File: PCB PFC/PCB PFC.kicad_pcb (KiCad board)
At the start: 2 copper layers, 44 parts, among them J1 INA_1, J2 INA_2, J4 External_Power, J5 BAT54S_1, J6 BAT54S_2, SW2 SW_Push, U2 L7805, U3 TL082, U4 TL084, U5 TL082, U8 ESP32-C3_SUPERMINI_TH

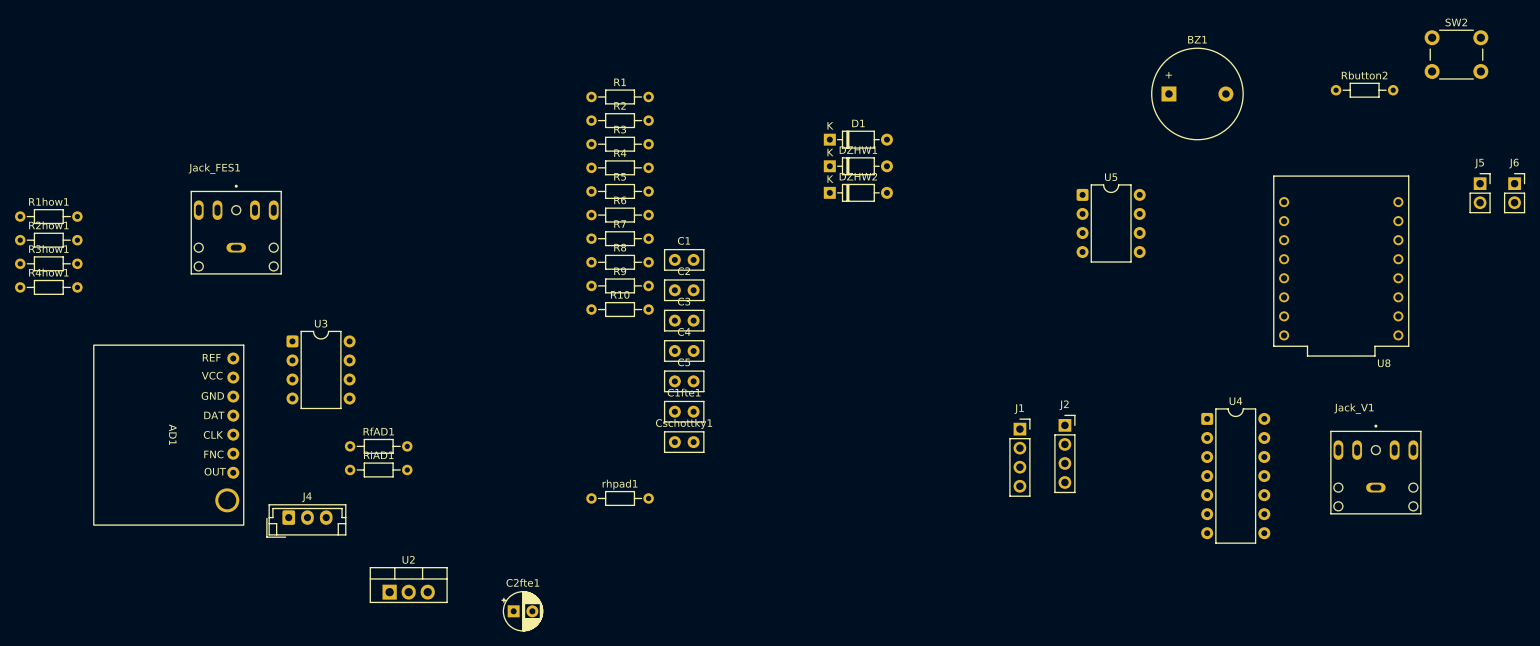
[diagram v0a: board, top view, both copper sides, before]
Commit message: Cambio valores a comerciales y agrego OpAmps SMD
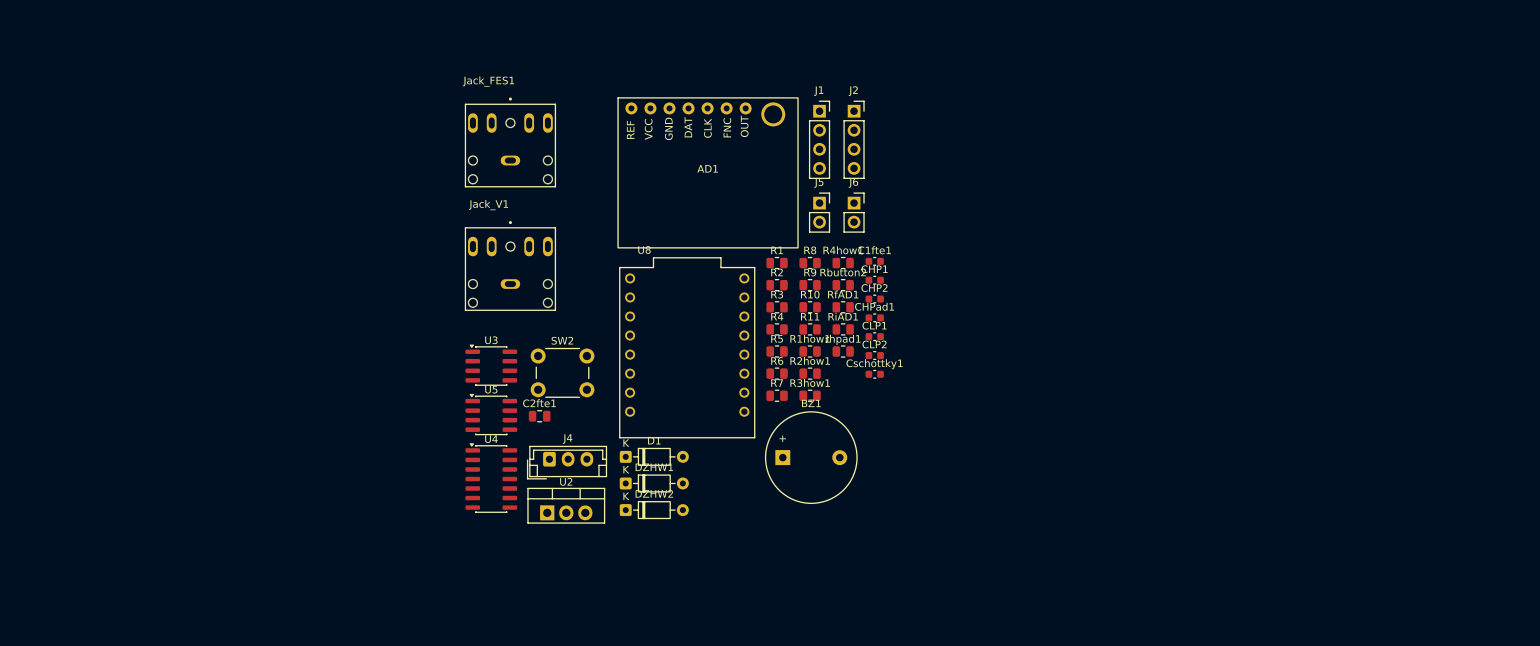
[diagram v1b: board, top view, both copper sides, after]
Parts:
- removed C1: C, Capacitor_THT:C_Disc_D5.0mm_W2.5mm_P2.50mm
- removed C2: 100n, Capacitor_THT:C_Disc_D5.0mm_W2.5mm_P2.50mm
- removed C3: 100p, Capacitor_THT:C_Disc_D5.0mm_W2.5mm_P2.50mm
- removed C4: 1.8n, Capacitor_THT:C_Disc_D5.0mm_W2.5mm_P2.50mm
- removed C5: 220p, Capacitor_THT:C_Disc_D5.0mm_W2.5mm_P2.50mm
- added CHP1: 4.7n, Capacitor_SMD:C_0603_1608Metric, F.Cu at (158.2, 85.3)
- added CHP2: 1.5n, Capacitor_SMD:C_0603_1608Metric, F.Cu at (158.2, 87.8)
- added CHPad1: 10uF, Capacitor_SMD:C_0603_1608Metric, F.Cu at (158.2, 90.4)
- added CLP1: 100p, Capacitor_SMD:C_0603_1608Metric, F.Cu at (158.2, 92.9)
- added CLP2: 270p, Capacitor_SMD:C_0603_1608Metric, F.Cu at (158.2, 95.4)
- added R11: 1k, Resistor_SMD:R_0805_2012Metric, F.Cu at (149.5, 91.9)
- C1fte1: footprint Capacitor_THT:C_Disc_D5.0mm_W2.5mm_P2.50mm -> Capacitor_SMD:C_0603_1608Metric
- C2fte1: footprint Capacitor_THT:CP_Radial_D5.0mm_P2.50mm -> Capacitor_SMD:C_0805_2012Metric
- Cschottky1: value 2,2n -> 4.7n; footprint Capacitor_THT:C_Disc_D5.0mm_W2.5mm_P2.50mm -> Capacitor_SMD:C_0603_1608Metric
- R1, R1how1, R2, R2how1, R3how1, R4, R4how1, R5, R6, R9, Rbutton2, RfAD1, RiAD1: footprint Resistor_THT:R_Axial_DIN0204_L3.6mm_D1.6mm_P7.62mm_Horizontal -> Resistor_SMD:R_0805_2012Metric
- R10: value 4k -> 4.7k; footprint Resistor_THT:R_Axial_DIN0204_L3.6mm_D1.6mm_P7.62mm_Horizontal -> Resistor_SMD:R_0805_2012Metric
- R3: value 50 -> 1k; footprint Resistor_THT:R_Axial_DIN0204_L3.6mm_D1.6mm_P7.62mm_Horizontal -> Resistor_SMD:R_0805_2012Metric
- R7: value 2.2k -> 1k; footprint Resistor_THT:R_Axial_DIN0204_L3.6mm_D1.6mm_P7.62mm_Horizontal -> Resistor_SMD:R_0805_2012Metric
- R8: value 11k -> 10k; footprint Resistor_THT:R_Axial_DIN0204_L3.6mm_D1.6mm_P7.62mm_Horizontal -> Resistor_SMD:R_0805_2012Metric
- U3, U5: footprint Package_DIP:DIP-8_W7.62mm -> Package_SO:SOIC-8_3.9x4.9mm_P1.27mm
- U4: footprint Package_DIP:DIP-14_W7.62mm -> Package_SO:SOIC-14_3.9x8.7mm_P1.27mm
- rhpad1: value 330 -> 500; footprint Resistor_THT:R_Axial_DIN0204_L3.6mm_D1.6mm_P7.62mm_Horizontal -> Resistor_SMD:R_0805_2012Metric
- moved SW2 126.6 mm to (113.3, 95.5)
- moved Jack_V1 118.6 mm to (109.6, 85.8)
- moved R4how1 109.8 mm to (153.9, 83.0)
- moved R1how1 106.9 mm to (149.5, 94.8)
- moved R2how1 106.8 mm to (149.5, 97.8)
- moved R3how1 106.8 mm to (149.5, 100.8)
- moved U4 95.8 mm to (107.0, 111.9)
- moved J5 88.1 mm to (150.8, 75.0)
- moved J6 88.1 mm to (155.4, 75.0)
- moved U8 88.1 mm to (133.2, 95.0), turned to 0 degrees
- moved U5 84.2 mm to (107.0, 103.4)
- moved AD1 80.0 mm to (135.9, 71.0), turned to 0 degrees
- moved BZ1 70.7 mm to (145.9, 109.0)
- moved Rbutton2 70.7 mm to (153.9, 86.0)
- moved RiAD1 68.4 mm to (153.9, 91.9)
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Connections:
- R7 pad 2: Net-(R7-Pad2) -> Net-(R11-Pad1)
- R8 pad 2: Net-(R7-Pad2) -> Net-(R11-Pad2)
- U4 pad 7: Net-(R7-Pad2) -> Net-(R11-Pad2)

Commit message: Placa final chidori 3V3 by Gus
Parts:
- removed C1fte1: 20pF, Capacitor_SMD:C_0603_1608Metric
- removed C2fte1: 10uFx16V, Capacitor_SMD:C_0805_2012Metric
- removed J1: INA_1, Connector_PinSocket_2.54mm:PinSocket_1x04_P2.54mm_Vertical
- removed J2: INA_2, Connector_PinSocket_2.54mm:PinSocket_1x04_P2.54mm_Vertical
- removed J6: BAT54S_2, Connector_PinSocket_2.54mm:PinSocket_1x02_P2.54mm_Vertical
- removed U2: L7805, Package_TO_SOT_THT:TO-220-3_Vertical
- added Cd_01: 22n, Capacitor_SMD:C_0603_1608Metric, B.Cu at (144.3, 76.3)
- added Cd_2: 22n, Capacitor_SMD:C_0603_1608Metric, B.Cu at (144.4, 85.8)
- added Cd_4: 22n, Capacitor_SMD:C_0603_1608Metric, B.Cu at (156.1, 85.6)
- added Cd_5: 22n, Capacitor_SMD:C_0603_1608Metric, B.Cu at (167.3, 84.4)
- added Cd_6: 22n, Capacitor_SMD:C_0603_1608Metric, B.Cu at (163.2, 82.3)
- added Cd_7: 22n, Capacitor_SMD:C_0603_1608Metric, B.Cu at (159.9, 110.4)
- added Cd_8: 22n, Capacitor_SMD:C_0603_1608Metric, B.Cu at (152.2, 103.7)
- added D2: BAT54S, Package_TO_SOT_SMD:SOT-23, B.Cu at (139.5, 97.1)
- added U1: INA128, Package_TO_SOT_SMD:SOT-23-8, B.Cu at (166.9, 82.0)
- CHP1, CHP2, CHPad1, CLP1, CLP2, Cschottky1, R1, R10, R11, R1how1, R2, R2how1, R3, R3how1, R4, R4how1, R5, R6, R7, R8, R9, Rbutton2, RfAD1, RiAD1, U3, U4, U5, rhpad1: moved to B.Cu
- J5: value BAT54S_1 -> JUMPER_BAT54S
- moved J4 60.6 mm to (172.3, 90.3), turned to 90 degrees
- moved U5 56.1 mm to (159.6, 83.8), turned to 90 degrees
- moved Jack_V1 55.3 mm to (162.3, 69.0), turned to 180 degrees
- moved U3 49.0 mm to (154.7, 108.1)
- moved U4 48.9 mm to (145.0, 81.1), turned to -90 degrees
- moved Jack_FES1 47.4 mm to (137.0, 108.0), turned to -90 degrees
- moved AD1 38.5 mm to (157.8, 102.7)
- moved BZ1 37.5 mm to (128.6, 75.8), turned to 90 degrees
- moved R7 32.3 mm to (146.2, 68.5), turned to 180 degrees
- moved DZHW2 28.0 mm to (147.7, 99.8)
- moved R11 25.9 mm to (146.2, 66.2)
- moved R6 25.3 mm to (146.2, 72.5)
- moved DZHW1 24.6 mm to (147.7, 103.0)
- moved Rbutton2 24.4 mm to (129.6, 88.1)
- moved CHP1 24.0 mm to (140.9, 68.7), turned to 180 degrees
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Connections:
- net /Fes Out+ renamed /FesOut+
- AD1 pad 2: /3v3 -> /+
- J5 pad 1: unconnected-(J5-Pin_1-Pad1) -> /CON_BAT54S
- J5 pad 2: unconnected-(J5-Pin_2-Pad2) -> /SIN_BAT54S
- R10 pad 2: Net-(R10-Pad2) -> /SIN_BAT54S
- SW2 pad 1: /3v3 -> /+
- U4 pad 14: Net-(R10-Pad2) -> /SIN_BAT54S
- U8 pad 2: /alarm -> unconnected-(U8-GPIO2-Pad2)
- U8 pad 3.3: /3v3 -> unconnected-(U8-3V3-Pad3.3)
- U8 pad 5: unconnected-(U8-GPIO5-Pad5) -> /alarm
- U8 pad 5V: /5V -> /+
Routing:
- net GNDREF: track 0.00 -> 252.4 mm, vias 0 -> 10
- net /+: track 0.00 -> 180.0 mm, vias 0 -> 4
- net /data: track 0.00 -> 137.4 mm, vias 0 -> 4
- net /fnc: track 0.00 -> 120.6 mm, vias 0 -> 2
- net /-: track 0.00 -> 91.8 mm, vias 0 -> 4
- net Net-(CHP1-Pad1): track 0.00 -> 43.8 mm, vias 0 -> 4
- net /outAD: track 0.00 -> 42.7 mm
- net /FesOut+: track 0.00 -> 35.8 mm
- net /Vout: track 0.00 -> 29.0 mm, vias 0 -> 2
- net Net-(R1how1-Pad1): track 0.00 -> 26.0 mm
- net Net-(CHP2-Pad1): track 0.00 -> 24.6 mm
- net Net-(U5A--): track 0.00 -> 22.7 mm, vias 0 -> 2
- net Net-(R11-Pad2): track 0.00 -> 22.4 mm
- net /clk: track 0.00 -> 21.2 mm
- net Net-(U4C--): track 0.00 -> 20.1 mm
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- added copper zone on B.Cu, net (none)
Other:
- board outline added: 59.9 x 57 mm
- board text added: "CHIDORI"

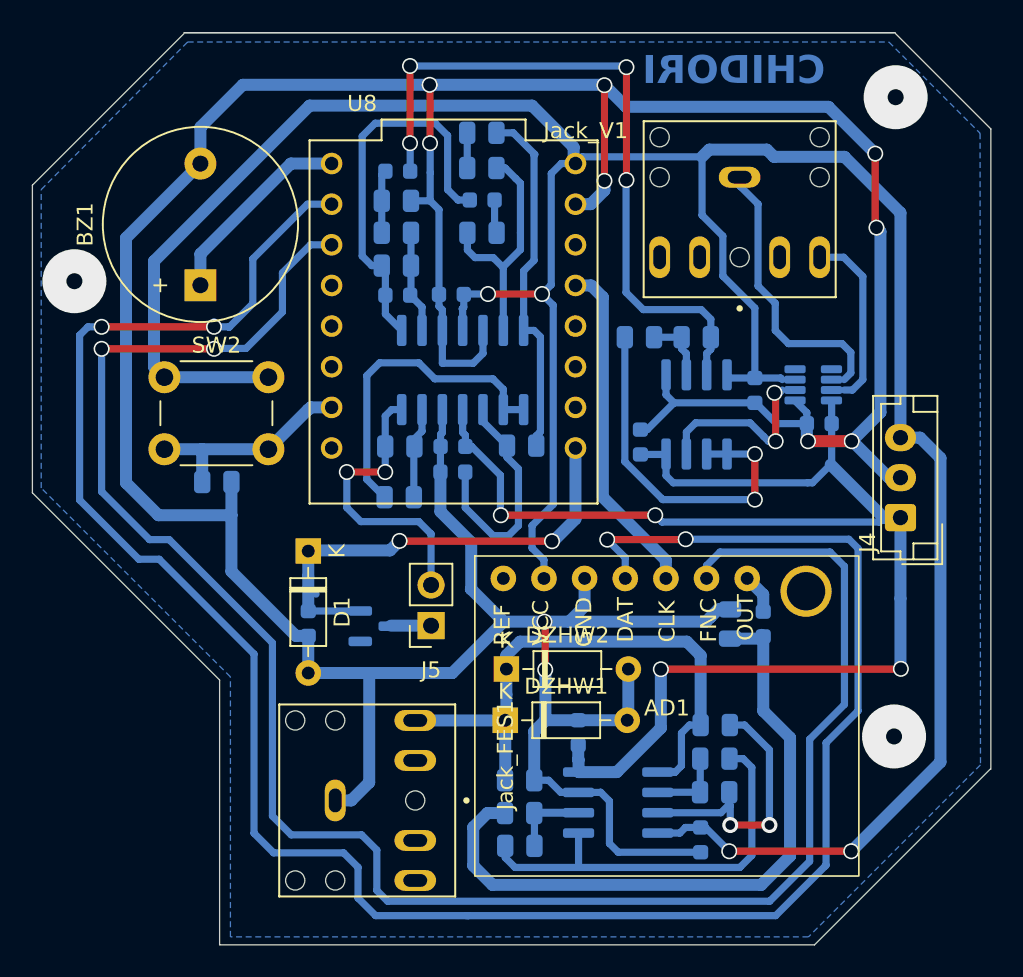
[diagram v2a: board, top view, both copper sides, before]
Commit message: actualizacion de placa y filtrado: correccion de ad9833 e ina + filtrado
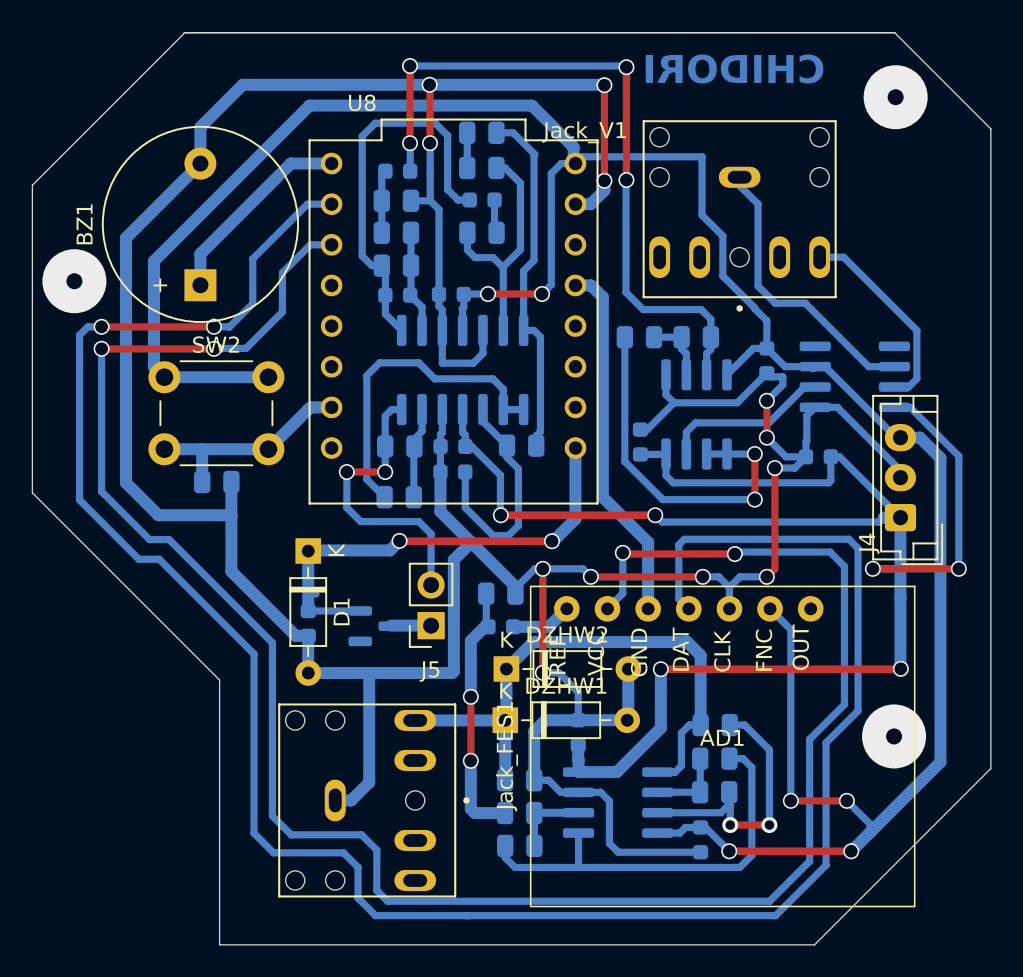
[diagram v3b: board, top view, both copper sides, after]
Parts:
- U1: footprint Package_TO_SOT_SMD:SOT-23-8 -> Package_SO:SOIC-8_3.9x4.9mm_P1.27mm
- moved CHPad1 16.4 mm to (147.4, 97.1), turned to 180 degrees
- moved rhpad1 14.5 mm to (147.4, 95.0), turned to 180 degrees
- moved AD1 3.97 mm to (161.2, 104.6)
- moved U1 2.65 mm to (169.5, 81.5)
- moved Cd_5 2.08 mm to (167.2, 86.5)
- moved Cd_6 2.00 mm to (164.0, 80.5)
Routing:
- net /outAD: track 42.7 -> 16.3 mm, vias 0 -> 2
- net /+: track 180.0 -> 160.3 mm, vias 4 -> 6
- net /-: track 91.8 -> 109.6 mm, vias 4 -> 6
- net GNDREF: track 252.4 -> 240.2 mm, vias 10 -> 12
- net /fnc: track 120.6 -> 128.7 mm, vias 2 -> 4
- net /data: track 137.4 -> 134.4 mm, vias 4 -> 2
- net /ECG+: track 11.1 -> 12.6 mm
- net /clk: track 21.2 -> 22.7 mm
- net Net-(AD1-OUT): track 2.49 -> 3.82 mm
- net /INAout: track 11.3 -> 10.6 mm, vias 2 -> 0
- net /FesOut+: track 35.8 -> 35.3 mm
- removed copper zone on B.Cu, net (none)

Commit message: Placa actualizada
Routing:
- added copper zone on B.Cu, net GNDREF
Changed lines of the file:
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@@
 			(outputformat 1)
 			(mirror no)
-			(drillshape 1)
+			(drillshape 0)
 			(scaleselection 1)
 			(outputdirectory "")
@@
 	(gr_line
 		(start 177.999788 66.008422)
-		(end 172.033037 60.041671)
+		(end 172.025 60)
 		(stroke
 			(width 0.05)
@@
 	(gr_line
 		(start 166.976917 117)
-		(end 177.953361 106.023556)
+		(end 177.999788 106.023586)
 		(stroke
 			(width 0.05)
@@
 	(gr_line
 		(start 166.976917 117)
-		(end 129.825 117)
+		(end 129.8 117)
 		(stroke
 			(width 0.05)
@@
 	)
 	(gr_line
-		(start 127.575 60.05)
+		(start 127.575 60)
 		(end 118.1 69.525)
 		(stroke
@@
 		(net 52)
 	)
+	(zone
+		(net 2)
+		(net_name "GNDREF")
+		(layer "B.Cu")
+		(hatch edge 0.5)
+		(connect_pads yes
+			(clearance 1)
+		)
+		(min_thickness 0.25)
+		(filled_areas_thickness no)
+		(fill yes
+			(thermal_gap 0.5)
+			(thermal_bridge_width 0.5)
+			(island_removal_mode 1)
+			(island_area_min 10)
+		)
+		(polygon
+			(pts
+				(xy 118.5 69.5) (xy 127.5 60.5) (xy 172 60.5) (xy 177.5 65.945185) (xy 178 105.5) (xy 166.5 117)
+				(xy 130 116.5) (xy 130 100) (xy 118.5 88.5)
+			)
+		)
+	)
 	(embedded_fonts no)
